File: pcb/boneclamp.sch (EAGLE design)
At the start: 10 parts, among them U1 AD7656YSTZ, U2 AD5754RBREZ, U3 SN74ABT541BDW, X1 F15-SHEILD

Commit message: Started working through the basic wiring on the schematic, connectrating on grounds, power, and analog IO
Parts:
- added C1, C3, C4: 1 uF, rcl:C-EUC0402
- added C10, C13, C5, C8: 10uF, rcl:C-USC0603
- added C11, C12, C14, C6, C7, C9: 0.1uF, rcl:C-EUC0603
- added JP2: (no value), jumper:JP2E
- added U4, U5: ADP3303ARZ-5, analog-devices-01:ADP3303ARZ-5
- C2: value (none) -> 1 uF; device rcl:C-EUC0603 -> rcl:C-EUC0402
- renumbered X1 to BCIO
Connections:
- new net AVCC: C7.1, C8.1, C9.1, U4.OUT, U4.OUT_2
- new net BB_5V: C10.1, C11.1, C5.1, C6.1, U$1.SYS_5V@1, U4.IN, U4.IN_2, U4.~SD, U5.IN, U5.IN_2, U5.~SD
- new net CONVST: U1.CONVST_A, U1.CONVST_B, U1.CONVST_C
- new net DGND: C10.2, C11.2, C13.2, C14.2, JP2.3, U$1.GND@6, U1.DGND, U1.DGND_2
- new net DVCC: C12.1, C13.1, C14.1, U5.OUT, U5.OUT_2
- new net N$10: C2.1, U1.REFCAPB
- new net N$11: C1.1, U1.REFCAPC
- new net N$12: JP2.2, U1.RANGE
- new net N$13: C4.1, U1.AVCC, U1.AVCC_2, U1.AVCC_3, U1.AVCC_4, U1.AVCC_5, U1.AVCC_6, U1.AVCC_7, U1.AVCC_8
- new net N$15: C12.2, U5.NR
- new net N$16: C7.2, U4.NR
- new net N$9: C3.1
- new net VDD_BB: U$1.VDD_5V@1
- new net VDRIVE: JP2.1, U$1.VDD_3V3EXP@1
- new net VSS: U1.VSS
- net AGND: now also C1.2, C2.2, C3.2, C4.2, C5.2, C6.2, C8.2, C9.2, U$1.GND@5, U1.AGND, U1.AGND_11, U1.AGND_2, U1.AGND_3, U1.AGND_4, U1.AGND_5, U1.AGND_6, U1.AGND_7, U1.AGND_8, U1.AGND_9, U4.GND, U5.GND

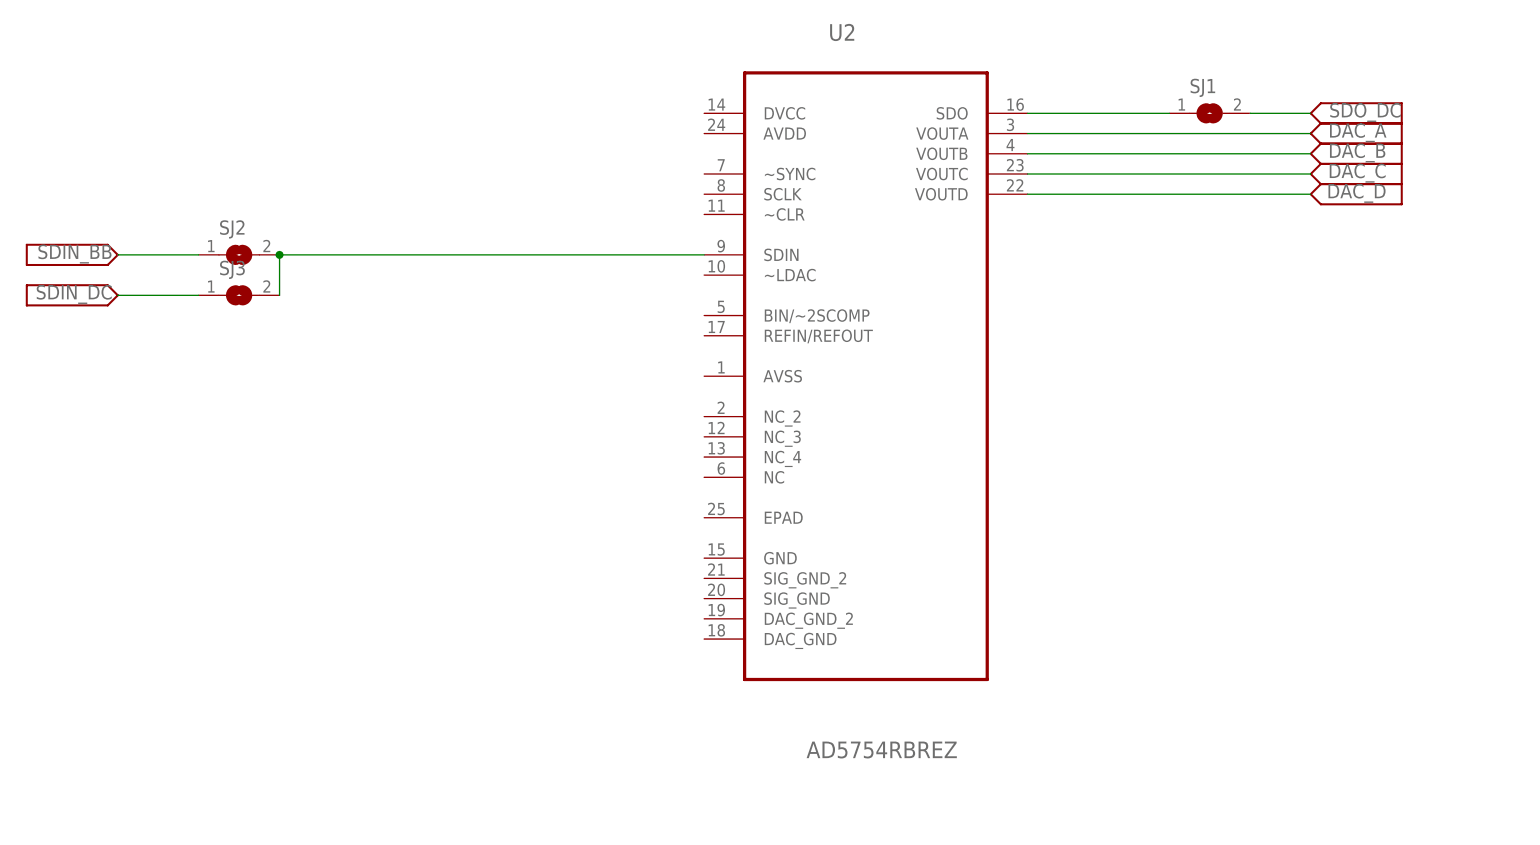
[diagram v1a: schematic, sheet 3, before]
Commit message: Added optional compensation comoponents and test points to DAC output lines. Added a right angle 0.1 inch pitch header for outside power input.
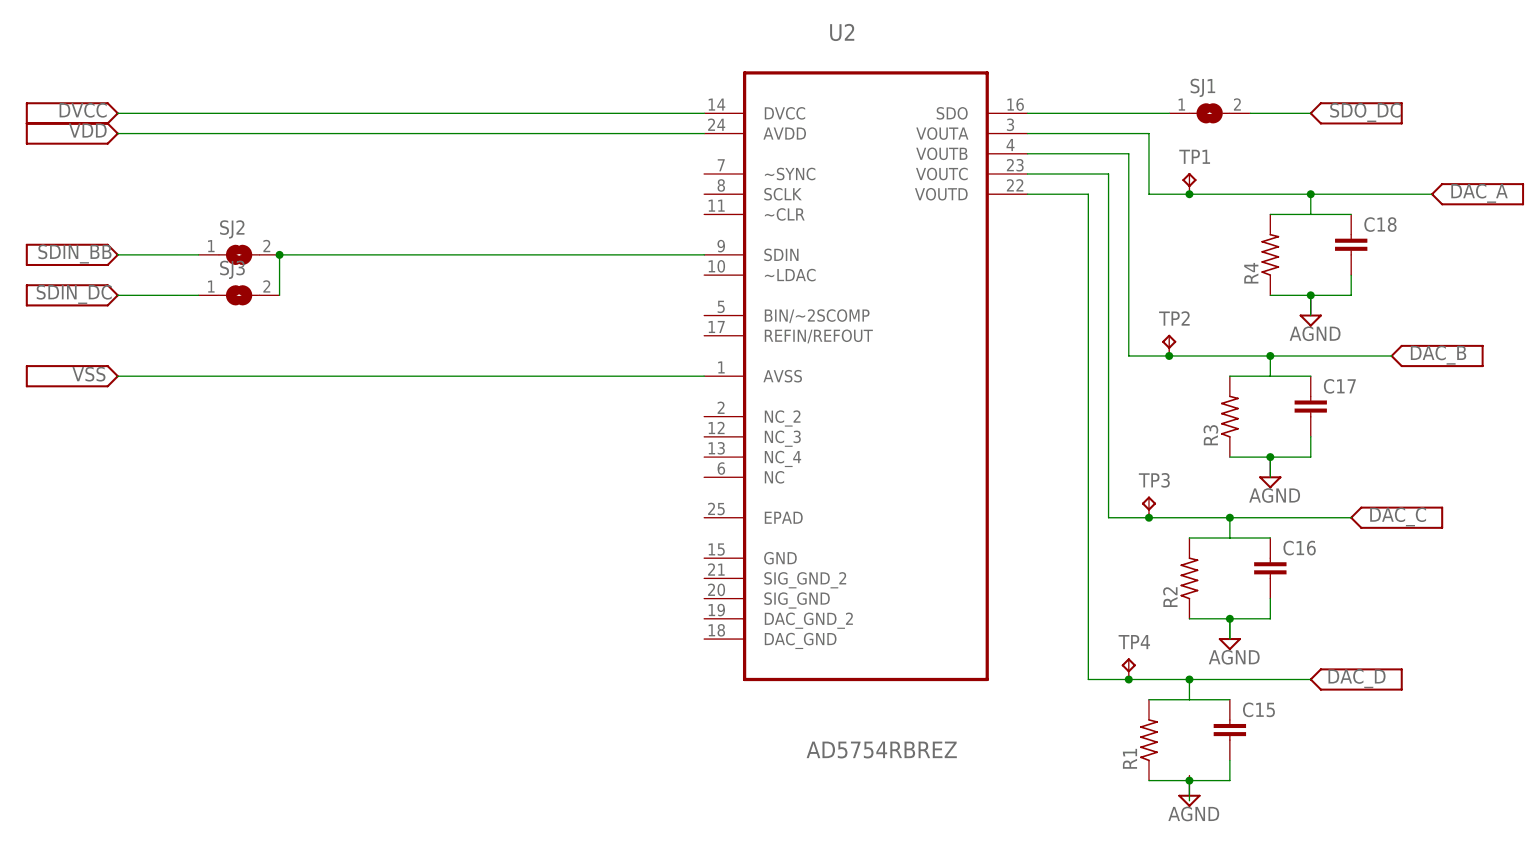
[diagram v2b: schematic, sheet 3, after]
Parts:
- added C15, C16, C17, C18: (no value), rcl:C-EUC0603
- added JP3: (no value), pinhead:PINHD-1X3/90
- added R1, R2, R3, R4: (no value), rcl:R-US_R0603
- added TP1, TP2, TP3, TP4: TPB1,27, testpad:TPB1,27
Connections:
- new net N$17: C15.2, R1.1
- new net VDD: U2.AVDD
- net AGND: now also C16.2, C17.2, C18.2, R2.1, R3.1, R4.1
- net DAC_A: now also C18.1, R4.2, TP1.TP
- net DAC_B: now also C17.1, R3.2, TP2.TP
- net DAC_C: now also C16.1, R2.2, TP3.TP
- net DAC_D: now also C15.1, R1.2, TP4.TP
- net DVCC: now also U2.DVCC
- net VSS: now also U2.AVSS

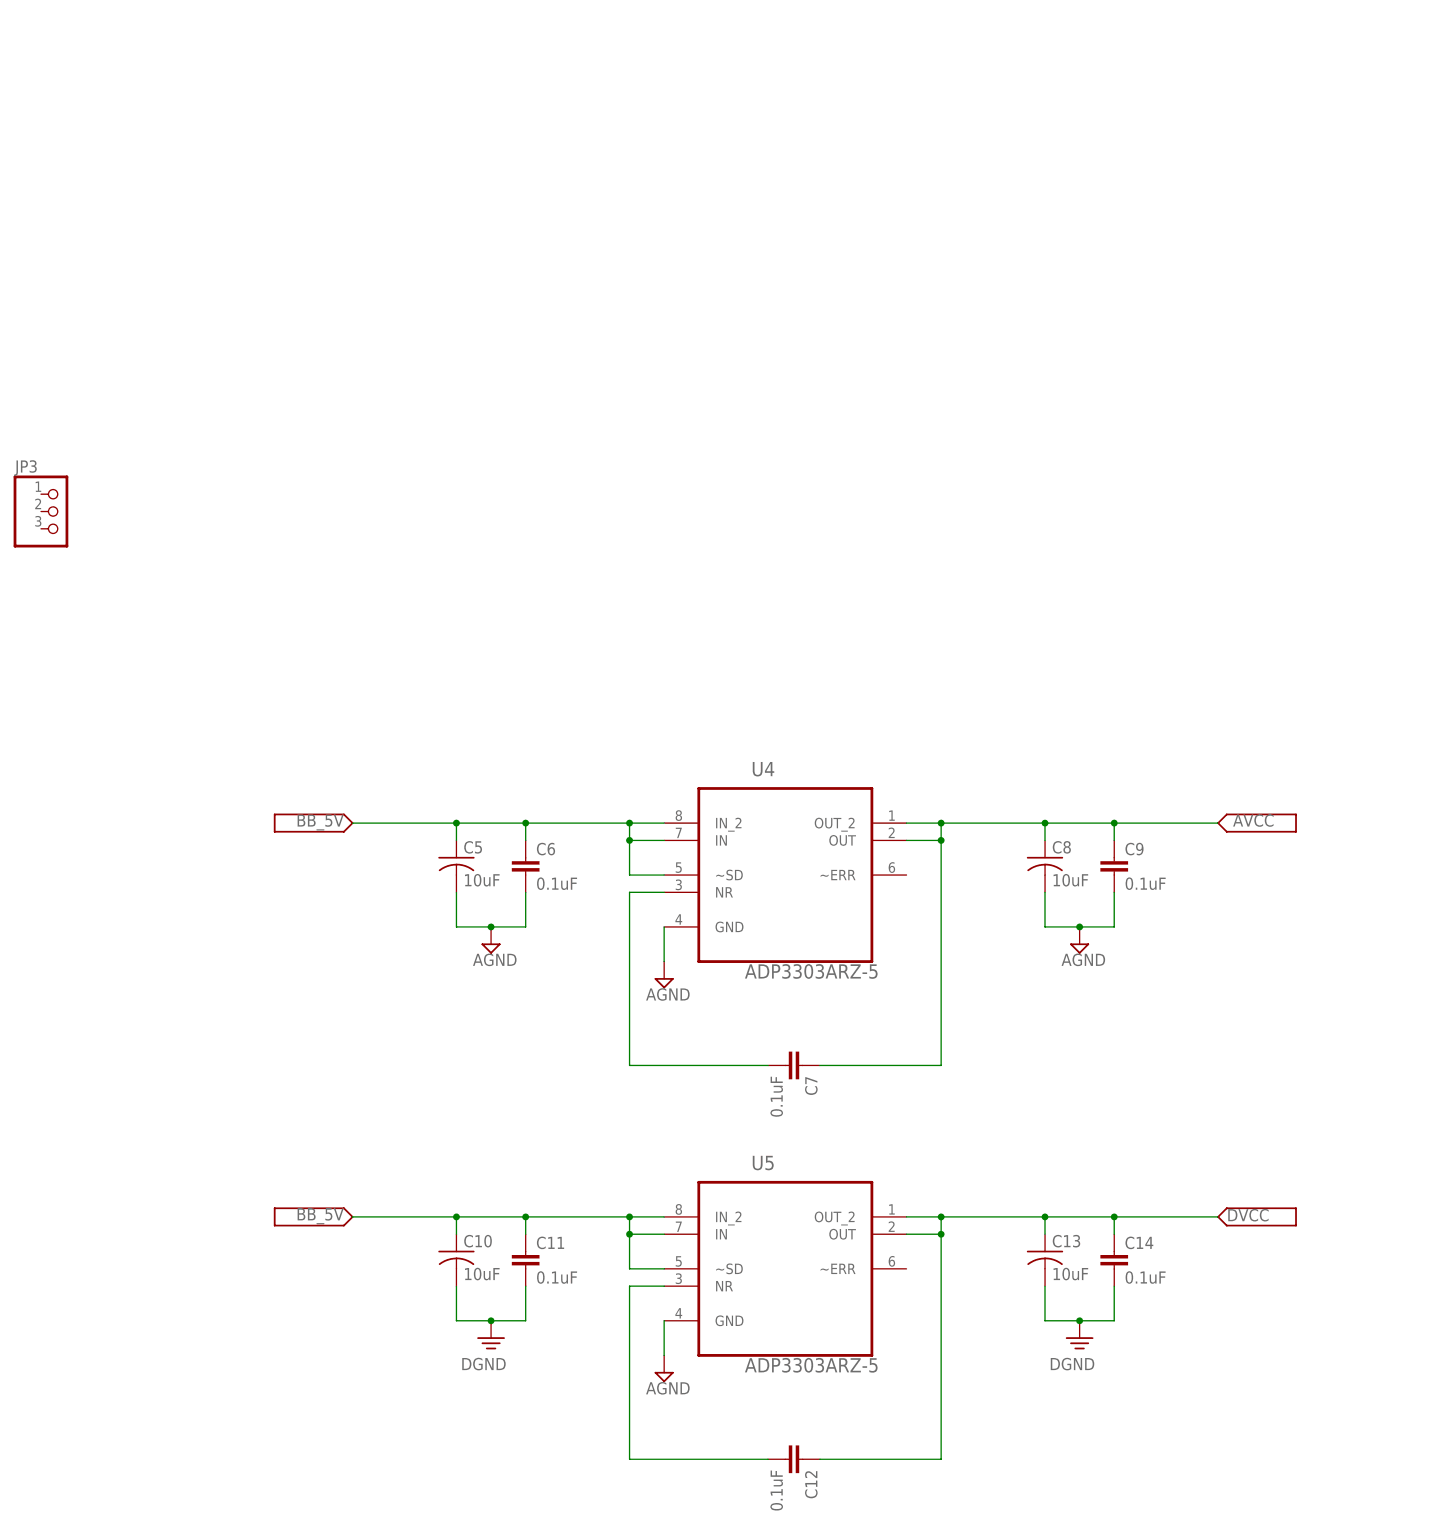
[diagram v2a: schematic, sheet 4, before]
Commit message: Found a good regulator for powering the BB using the +/- 6 to 12 volt rails required to use the boneclamp. Updated schematic and added data sheet to data-sheets folder
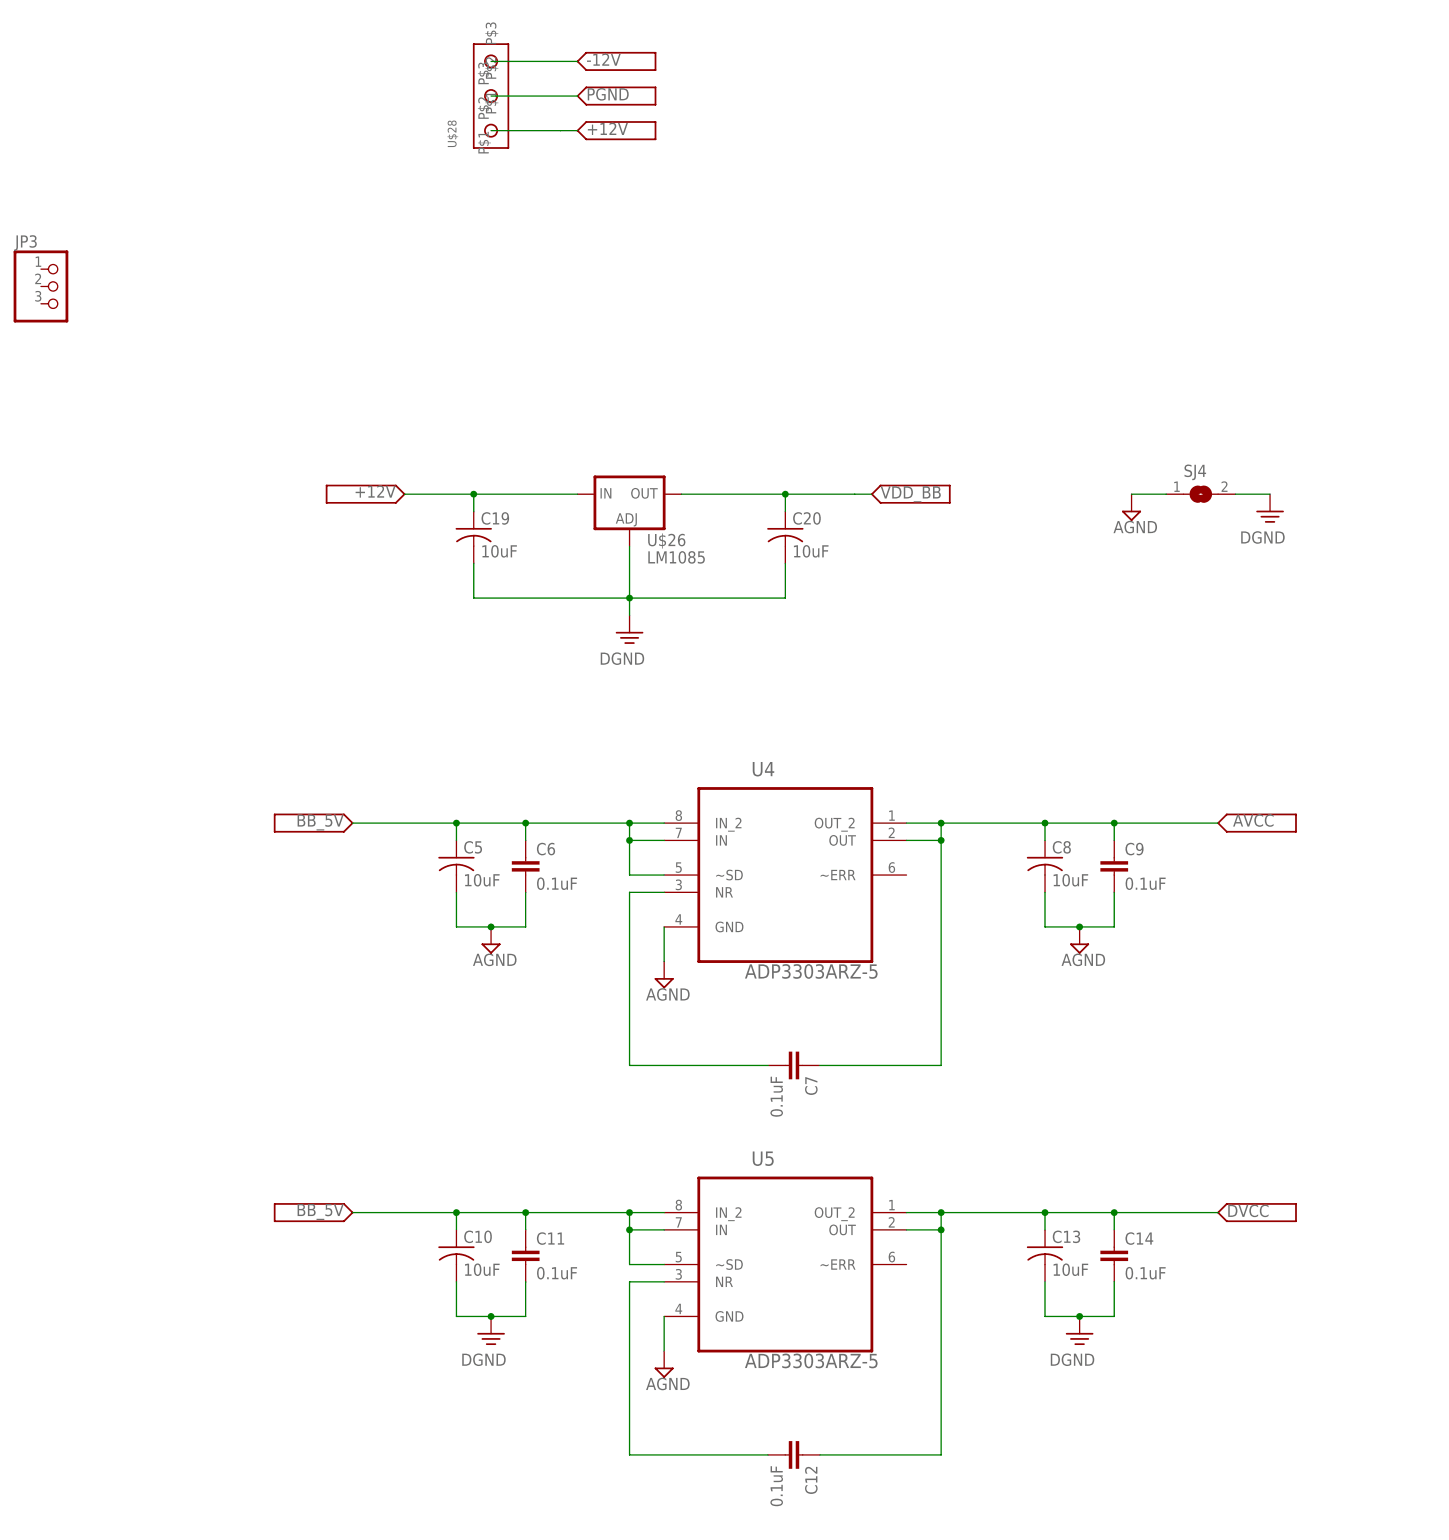
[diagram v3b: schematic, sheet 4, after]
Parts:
- added C19, C20: 10uF, rcl:C-USC1206
- added SJ4: (no value), jumper:SJ
- added U$26: LM1085, boneclamp:LM1085
- added U$28: SCREW3, boneclamp:SCREW3
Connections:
- new net +12V: C19.1, U$26.IN
- new net -12V: U$28.P$3
- new net PGND: U$28.P$2
- net AGND: now also SJ4.1
- net DGND: now also C19.2, C20.2, SJ4.2, U$26.ADJ
- net VDD_BB: now also C20.1, U$26.OUT
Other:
- moved on the sheet: BCIO, C10, C11, C12, C13, C14, JP1, JP2, JP3, U5

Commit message: Added EEPROM to the I2C2bus to follow standard daughter board device ID requirements
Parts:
- added C22: 0.1uF, rcl:C-EUC0603
- added IC1: 24C, on-semiconductor-01:24C
- added R10, R6: 5.6k, rcl:R-US_R0603
- added R11: 10k, rcl:R-US_R0603
- added R7, R8, R9: 4.75k, rcl:R-US_R0603
- added S1: SWS002, smd-special:SWS002
- added SJ5: (no value), jumper:SJ
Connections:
- new net I2C2_SCL: IC1.SCL, R10.1, U$1.I2C2_SCL
- new net I2C2_SDA: IC1.SDA, R6.1, U$1.I2C2_SDA
- new net N$14: IC1.A0, R7.1, R8.1, S1.1
- new net N$18: IC1.A1, S1.2
- new net N$19: IC1.A2, R9.1
- new net N$21: IC1.WP, SJ5.1
- new net N$22: R11.1, SJ5.2
- net BB_5V: now also U$1.SYS_5V@2
- net DGND: now also C22.2, IC1.GND, S1.3, S1.4
- net VDD_BB: now also U$1.VDD_5V@2
- net VDRIVE: now also C22.1, IC1.VCC, R10.2, R11.2, R6.2, R7.2, R8.2, R9.2, U$1.VDD_3V3EXP@2

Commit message: Added external 2.5 volt references for DAC and ADC. This circuit needs a buffer option which can be feed into the 3 position jumper.
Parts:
- added C23: 10uF, rcl:C-USC1206
- added C24, C26, C27: 0.1uF, rcl:C-EUC0603
- added JP4, JP6: (no value), jumper:JP1E
- added JP5: (no value), jumper:JP2E
- added TP5: TPB1,27, testpad:TPB1,27
- added U6: ADR431BRZ, analog-devices-01:ADR431BRZ
- C10, C13, C5, C8: device rcl:C-USC0603 -> rcl:C-USC1206
- JP3: device pinhead:PINHD-1X3/90 -> jumper:JP1E
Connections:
- new net N$20: JP3.1, U1.REFIN/REFOUT
- new net N$23: JP6.1
- new net N$24: JP4.1, U2.REFIN/REFOUT
- new net N$25: C26.1, U6.TP_2
- new net VREF_2.5V: JP3.2, JP4.2, JP5.2
- new net VREF_OUT: C27.1, JP5.3, JP6.2, TP5.TP, U6.VOUT
- net AGND: now also C10.2, C23.2, C24.2, C26.2, U6.GND; no longer C8.2
- net AVCC: now also C10.1; no longer C8.1
- net BB_5V: now also C8.1; no longer C10.1
- net DGND: now also C8.2; no longer C10.2
- net VDD: now also C23.1, C24.1, U6.VIN

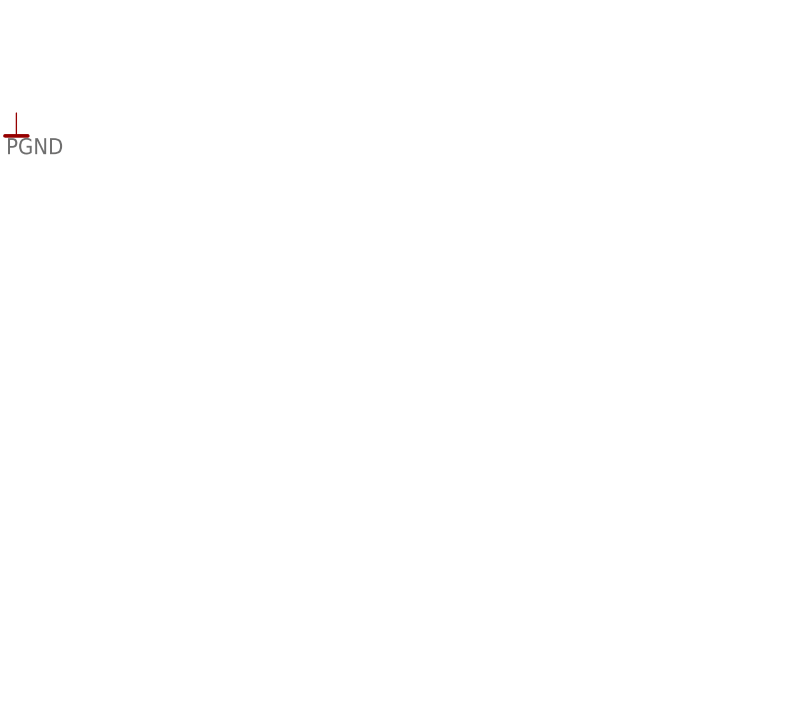
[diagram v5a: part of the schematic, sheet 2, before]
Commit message: Added new data sheets. Started a second pcb layout for new DAC/ADC unipolar solutions.
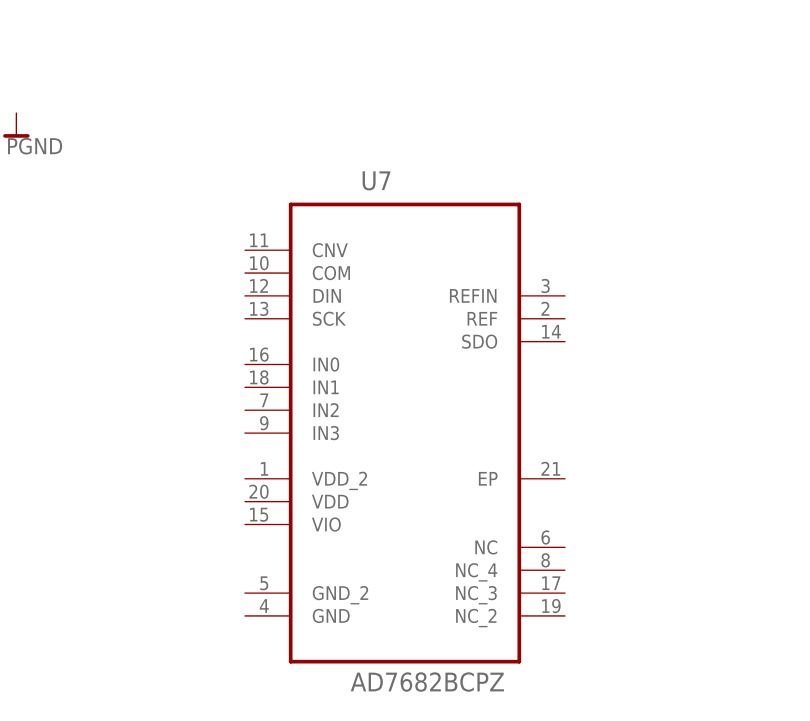
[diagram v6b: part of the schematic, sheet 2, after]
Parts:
- added U$42: AD5686RARUZ, analog-devices-02:AD5686RARUZ
- added U7: AD7682BCPZ, analog-devices-02:AD7682BCPZ
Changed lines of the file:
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@@
 <setting verticaltext="up"/>
 </settings>
-<grid distance="0.025" unitdist="inch" unit="inch" style="lines" multiple="1" display="yes" altdistance="0.01" altunitdist="inch" altunit="inch"/>
+<grid distance="0.1" unitdist="inch" unit="inch" style="lines" multiple="1" display="no" altdistance="0.01" altunitdist="inch" altunit="inch"/>
 <layers>
 <layer number="1" name="Top" color="4" fill="1" visible="no" active="no"/>
@@
 <part name="JP5" library="jumper" deviceset="JP2E" device=""/>
 <part name="JP6" library="jumper" deviceset="JP1E" device=""/>
+<part name="U$42" library="analog-devices-02" deviceset="AD5686RARUZ" device=""/>
+<part name="U7" library="analog-devices-02" deviceset="AD7682BCPZ" device=""/>
 </parts>
 <sheets>
@@
 <instance part="U$43" gate="G$1" x="-30.48" y="81.28" rot="R180"/>
 <instance part="U$44" gate="G$1" x="157.48" y="96.52"/>
+<instance part="U7" gate="A" x="73.66" y="-88.9"/>
 </instances>
 <busses>
@@
 <instance part="JP4" gate="A" x="33.02" y="55.88" rot="MR0"/>
 <instance part="U$45" gate="G$1" x="-20.32" y="53.34" rot="R180"/>
+<instance part="U$42" gate="G$1" x="73.66" y="124.46"/>
 </instances>
 <busses>
